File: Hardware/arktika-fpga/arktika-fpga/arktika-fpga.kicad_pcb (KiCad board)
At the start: 2 copper layers, 133.2 x 81.3 mm, 152 parts

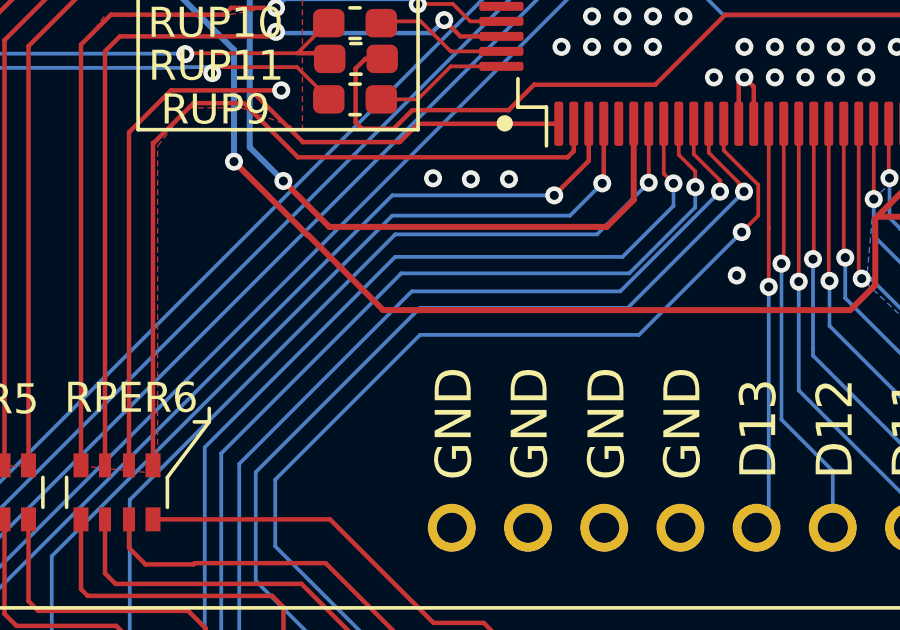
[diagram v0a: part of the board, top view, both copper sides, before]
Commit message: Fixed clearance error on design. Sent to fab
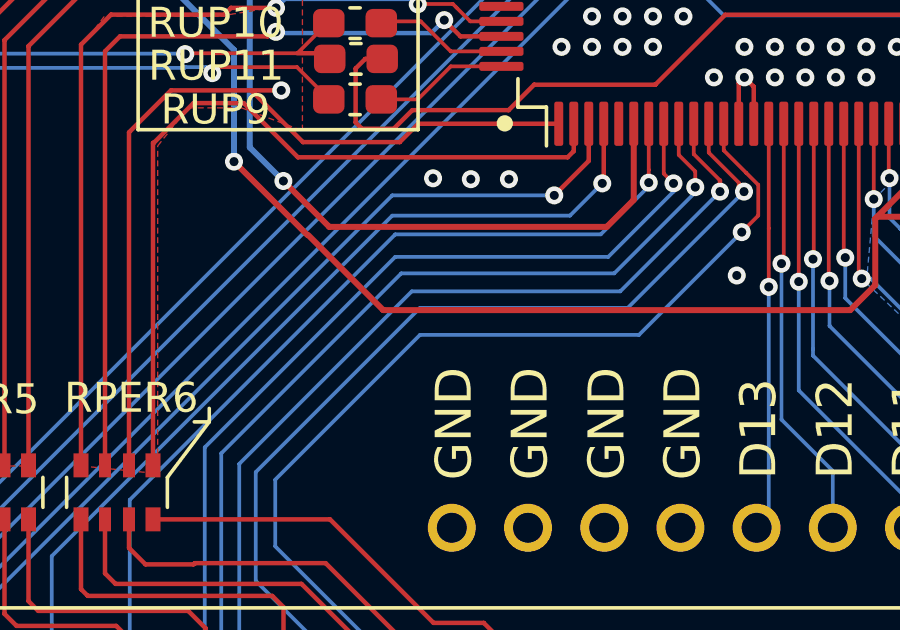
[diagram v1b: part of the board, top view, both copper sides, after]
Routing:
- net GND: vias 225 -> 233
- net (no net): vias 11 -> 3

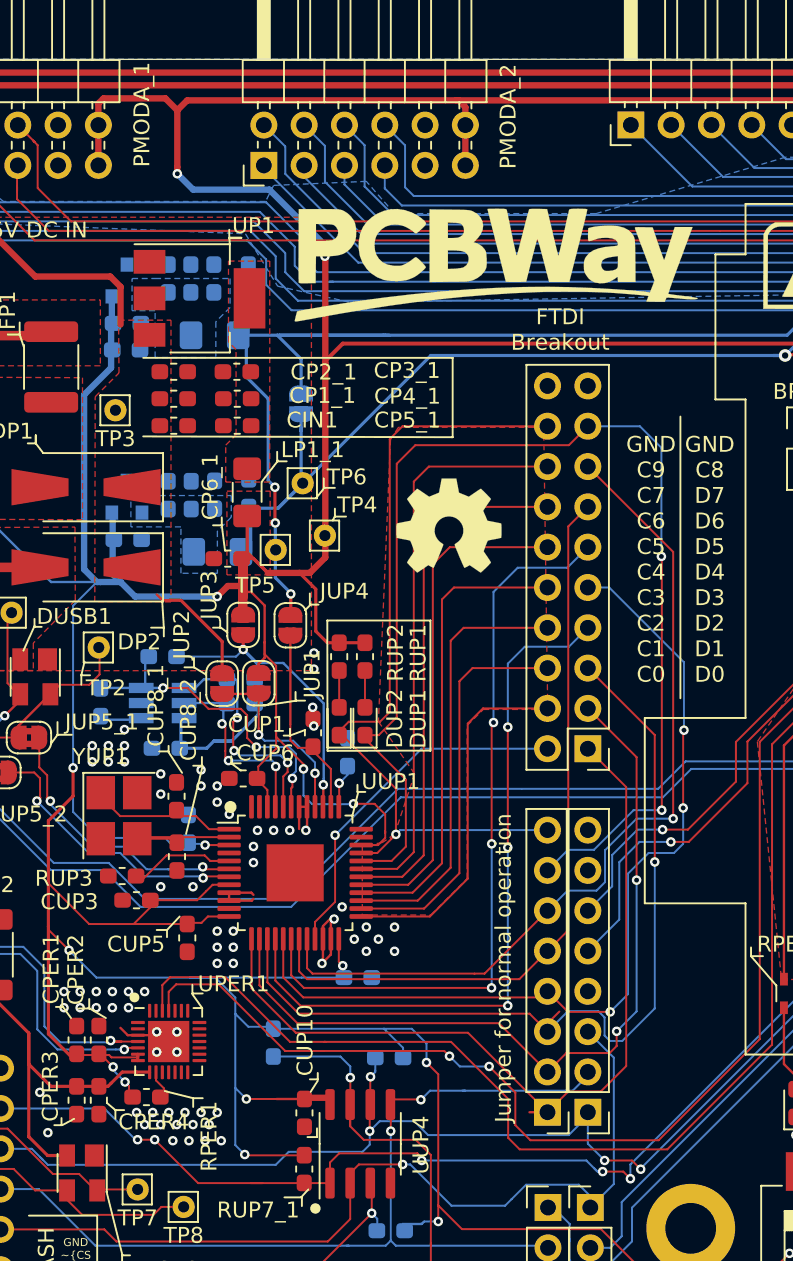
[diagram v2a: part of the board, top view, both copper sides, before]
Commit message: Fixed flash CS net
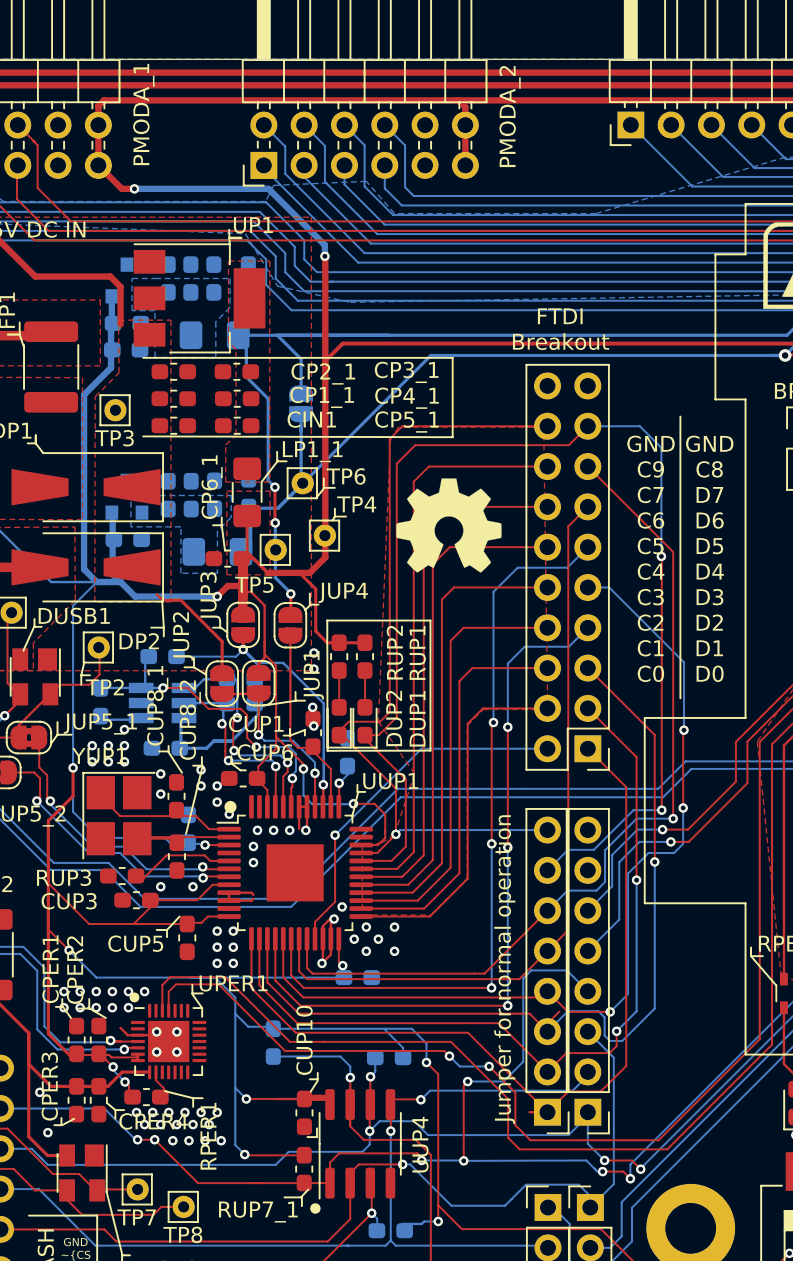
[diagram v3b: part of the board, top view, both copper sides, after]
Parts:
- removed the G*** at (126.0, 70.3)
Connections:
- JUP7_2 pad 4: /USB AND PROG/ICE_CS -> /USB AND PROG/FLASH_CS
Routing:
- net /USB AND PROG/FLASH_CS: track 112.3 -> 131.5 mm, vias 6 -> 8
